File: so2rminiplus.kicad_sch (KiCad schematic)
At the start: 73 parts, among them J1 STX-3000, J10 Conn_01x10_Pin, J11 Conn_01x03_Pin, J12 STX-3000, J13 STX-3000, J14 Conn_01x02_Pin, J15 Conn_01x02_Pin, J2 STX-3000, J3 STX-3000, J4 STX-3000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

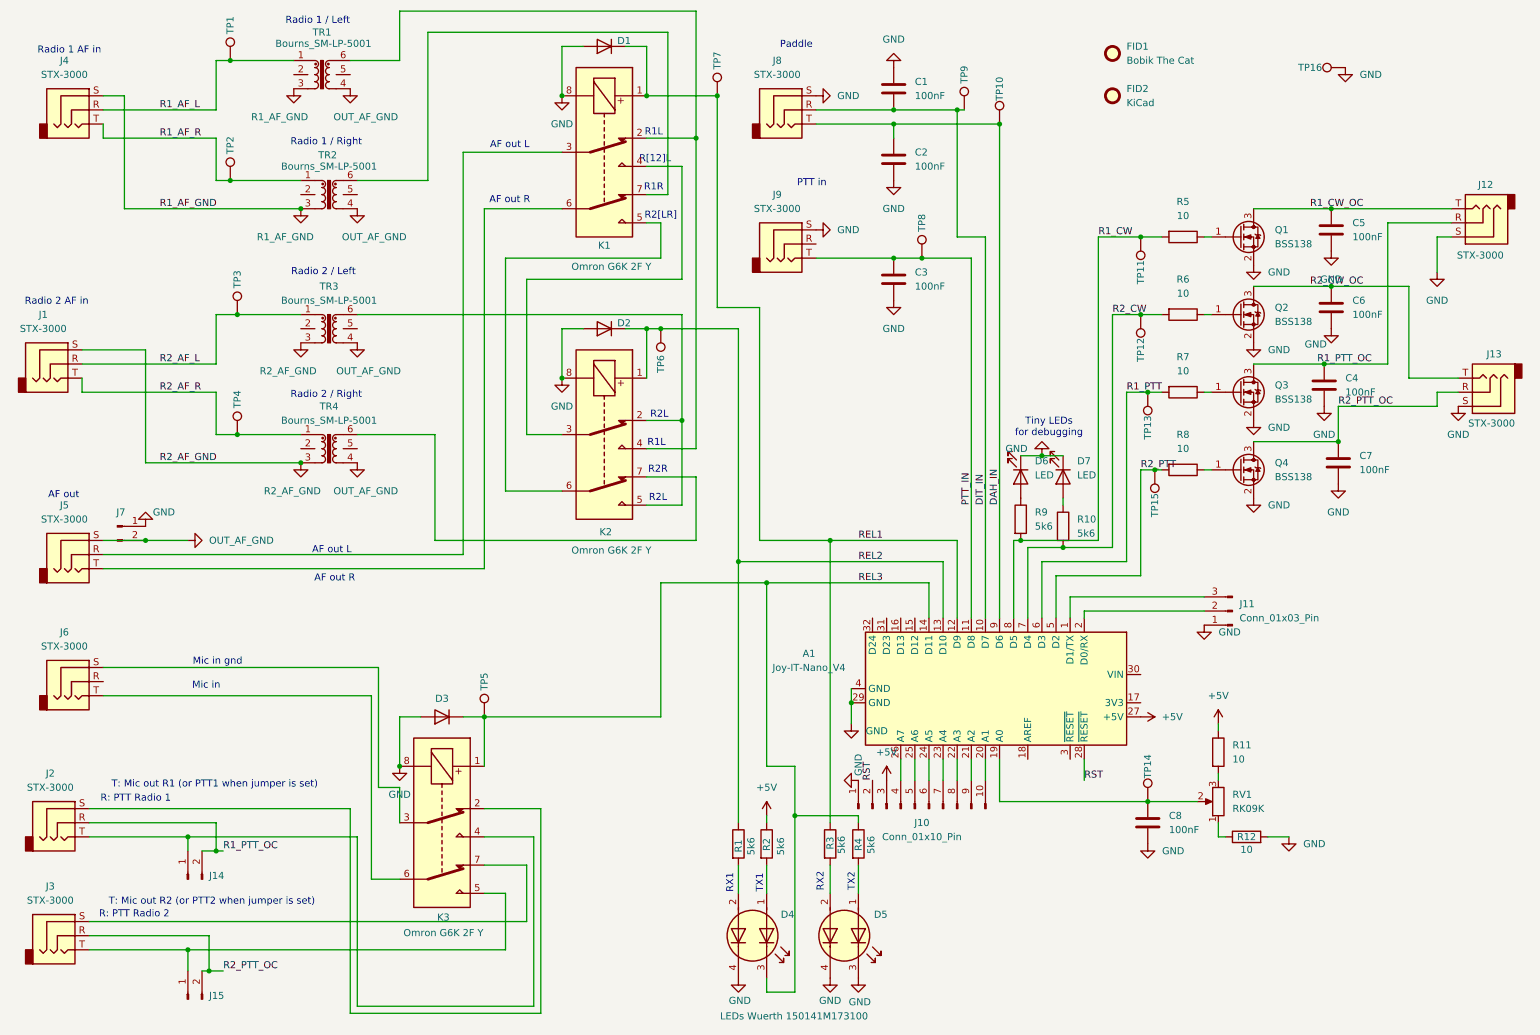
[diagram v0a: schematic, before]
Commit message: Fix: Use correct part number for WUE dual colour LED
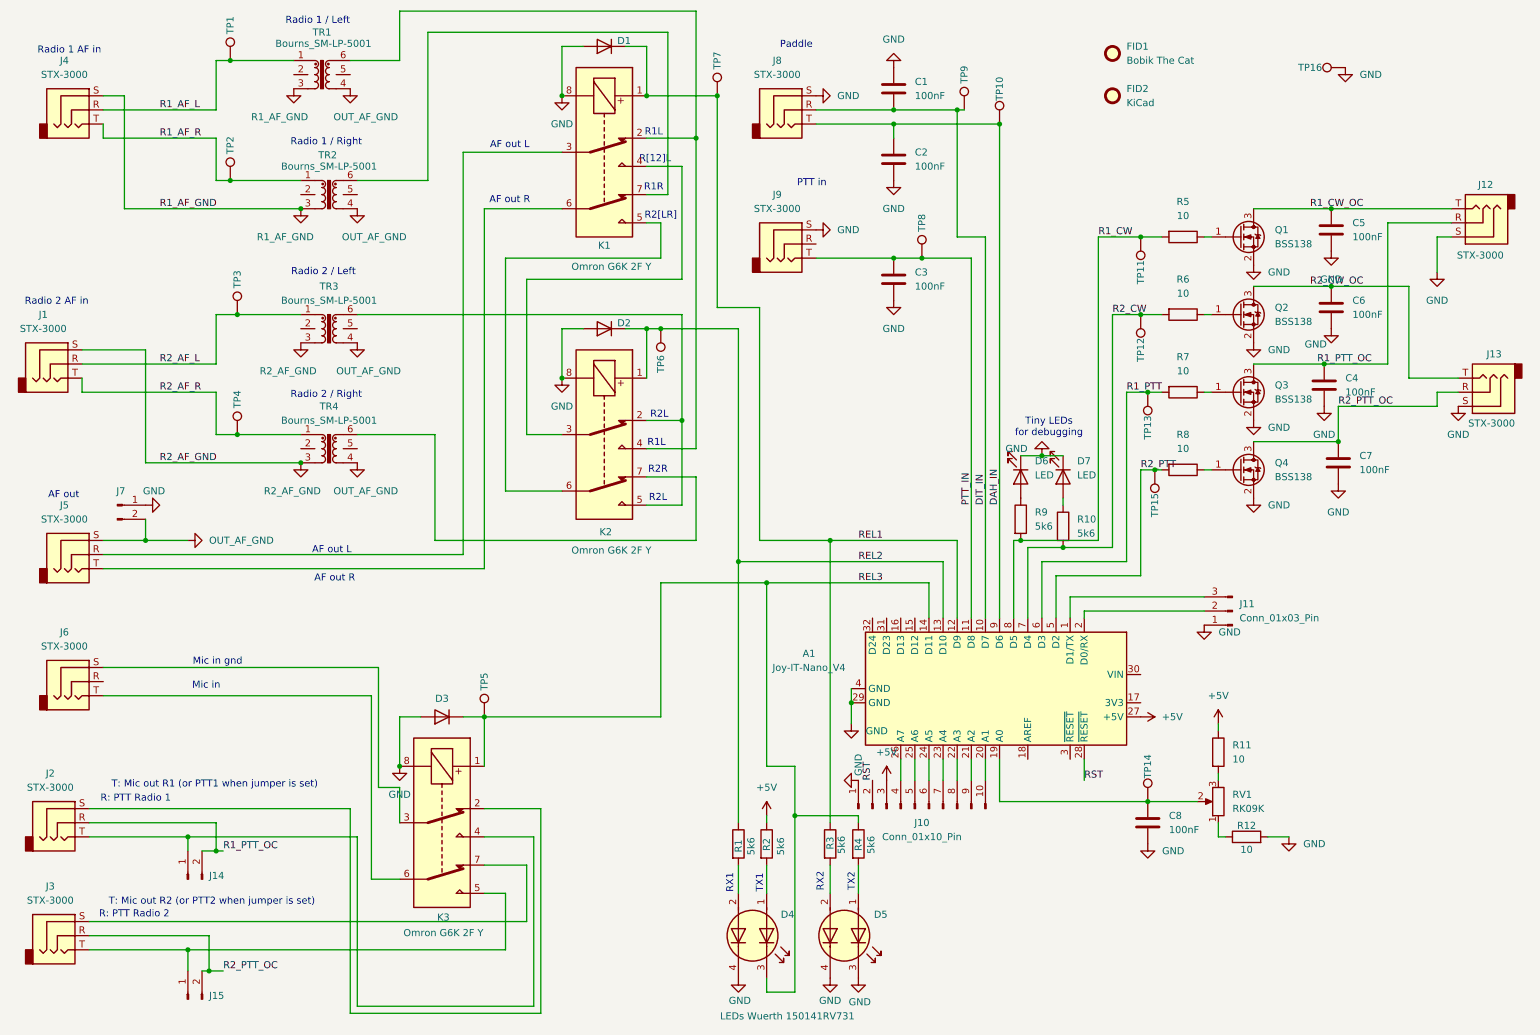
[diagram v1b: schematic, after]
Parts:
- D4: value LEDs Wuerth 150141M173100 -> LEDs Wuerth 150141RV731
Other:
- moved on the sheet: J7

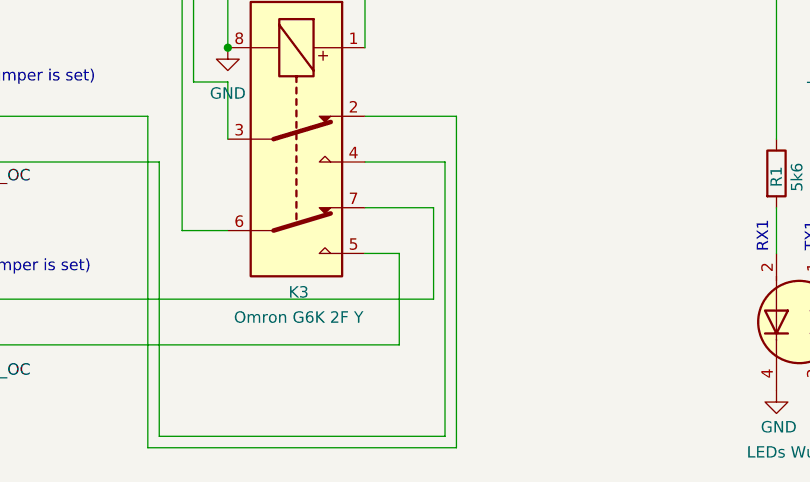
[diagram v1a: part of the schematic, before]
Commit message: Fix swapped pins 4 and 7 on relay K3.
Thanks to Peter, LA7WRA / LZ1VPC for finding this!
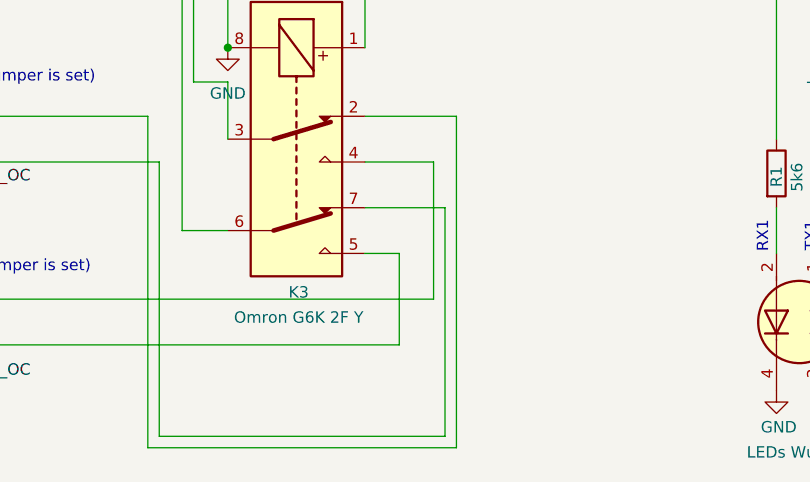
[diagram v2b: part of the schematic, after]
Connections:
- net at J14.1 (Pin_1), J2.T: now also K3.7; no longer K3.4
- net at J3.S: now also K3.4; no longer K3.7
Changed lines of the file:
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@@
 	(title_block
 		(title "SO2R MiniPlus")
-		(date "2025-12-18")
-		(rev "Rev 2b")
+		(date "2025-12-28")
+		(rev "Rev 2c")
 		(company "DJ5CW / SO5CW")
 	)
@@
 			(width 0)
 			(type default)
+			(color 9 0 255 1)
 		)
 	)
@@
 	(wire
 		(pts
-			(xy 96.52 167.64) (xy 104.14 167.64)
-		)
-		(stroke
-			(width 0)
-			(type default)
-		)
-	)
-	(wire
-		(pts
 			(xy 132.08 87.63) (xy 125.73 87.63)
 		)
@@
 	(wire
 		(pts
-			(xy 96.52 162.56) (xy 105.41 162.56)
-		)
-		(stroke
-			(width 0)
-			(type default)
-		)
-	)
-	(wire
-		(pts
 			(xy 45.72 186.69) (xy 46.99 186.69)
 		)
@@
 			(width 0)
 			(type default)
+			(color 9 0 255 1)
 		)
 	)
@@
 			(width 0)
 			(type default)
+			(color 9 0 255 1)
 		)
 	)
@@
 	(wire
 		(pts
+			(xy 104.14 162.56) (xy 96.52 162.56)
+		)
+		(stroke
+			(width 0)
+			(type default)
+			(color 9 0 255 1)
+		)
+	)
+	(wire
+		(pts
 			(xy 48.26 68.58) (xy 52.07 68.58)
 		)
@@
 			(width 0)
 			(type default)
+			(color 9 0 255 1)
 		)
 	)
@@
 	(wire
 		(pts
+			(xy 105.41 167.64) (xy 105.41 193.04)
+		)
+		(stroke
+			(width 0)
+			(type default)
+		)
+	)
+	(wire
+		(pts
 			(xy 204.47 123.19) (xy 204.47 121.92)
 		)
@@
 			(width 0)
 			(type default)
+			(color 9 0 255 1)
 		)
 	)
@@
 	(wire
 		(pts
-			(xy 104.14 167.64) (xy 104.14 177.8)
-		)
-		(stroke
-			(width 0)
-			(type default)
+			(xy 104.14 162.56) (xy 104.14 177.8)
+		)
+		(stroke
+			(width 0)
+			(type default)
+			(color 9 0 255 1)
 		)
 	)
@@
 			(width 0)
 			(type default)
+			(color 9 0 255 1)
 		)
 	)
@@
 			(width 0)
 			(type default)
+			(color 9 0 255 1)
 		)
 	)
@@
 	(wire
 		(pts
-			(xy 105.41 162.56) (xy 105.41 193.04)
-		)
-		(stroke
-			(width 0)
-			(type default)
-		)
-	)
-	(wire
-		(pts
 			(xy 110.49 49.53) (xy 96.52 49.53)
 		)
@@
 	(wire
 		(pts
+			(xy 96.52 167.64) (xy 105.41 167.64)
+		)
+		(stroke
+			(width 0)
+			(type default)
+		)
+	)
+	(wire
+		(pts
 			(xy 81.28 13.97) (xy 134.62 13.97)
 		)
@@
 			(width 0)
 			(type default)
+			(color 9 0 255 1)
 		)
 	)
@@
 			(width 0)
 			(type default)
+			(color 9 0 255 1)
 		)
 	)
@@
 			(width 0)
 			(type default)
-		)
-	)
+			(color 9 0 255 1)
+		)
+	)
